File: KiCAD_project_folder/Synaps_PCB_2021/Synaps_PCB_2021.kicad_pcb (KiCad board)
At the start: 4 copper layers, 101.6 x 101.6 mm, 56 parts, among them IC2 ESP32-S2, J1 USB_C_Receptacle, U1 MAX14748BEWW+, U2 CD74HC4067M, U3 AT25DF041x-UxN-x

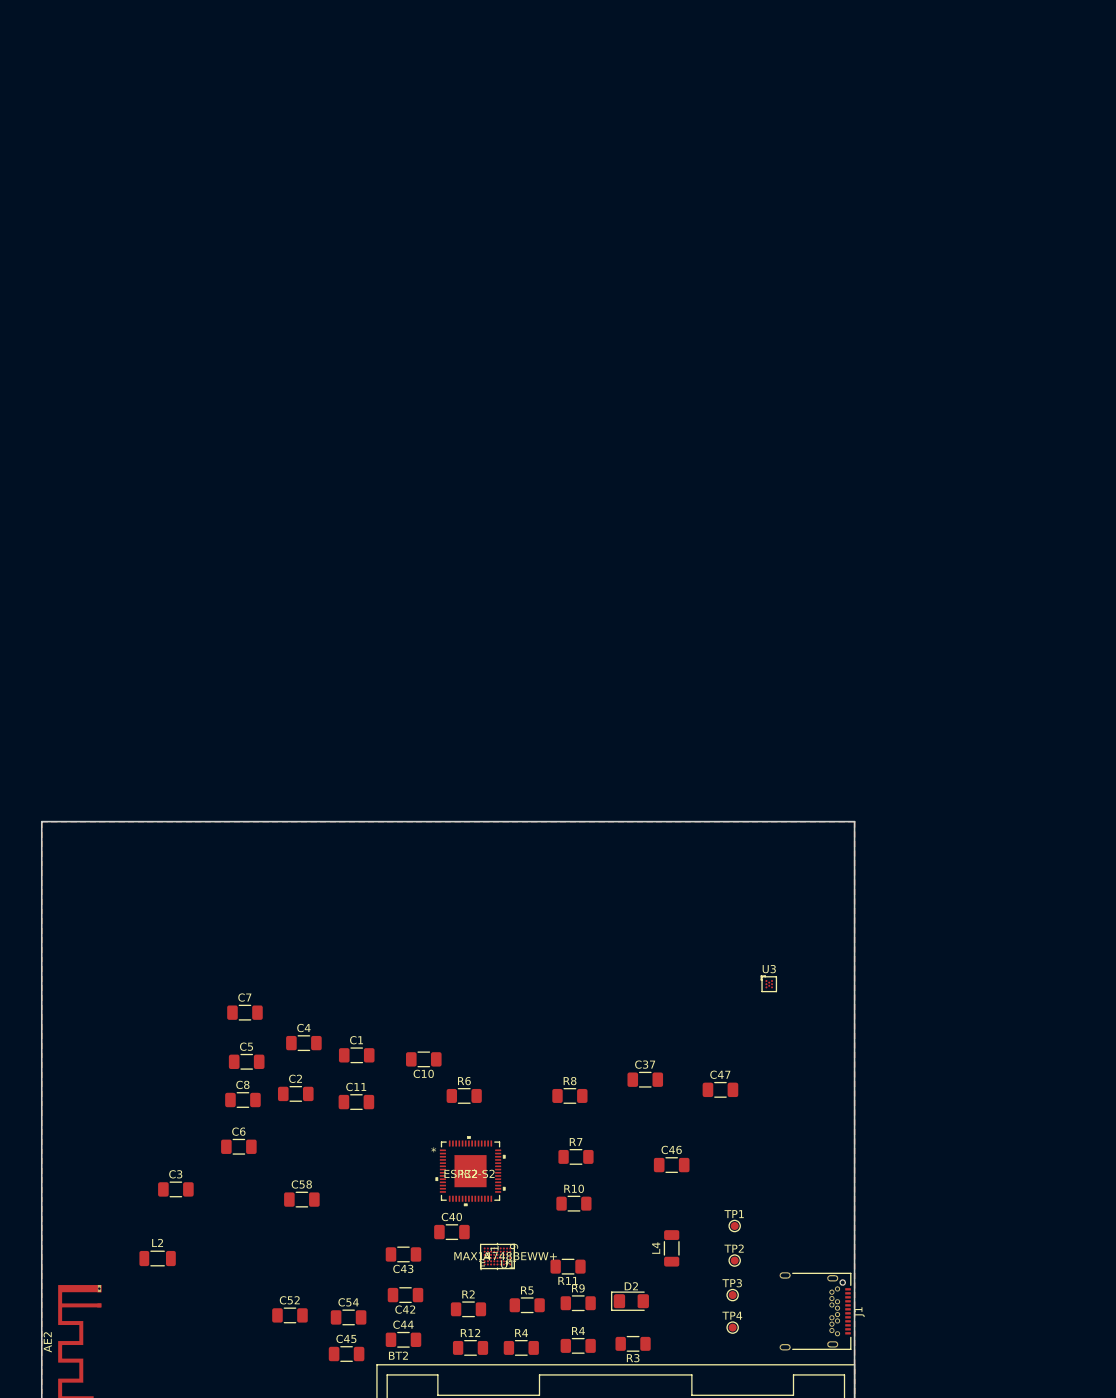
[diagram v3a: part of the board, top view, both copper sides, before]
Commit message: Updated pcb editor with the new components imported
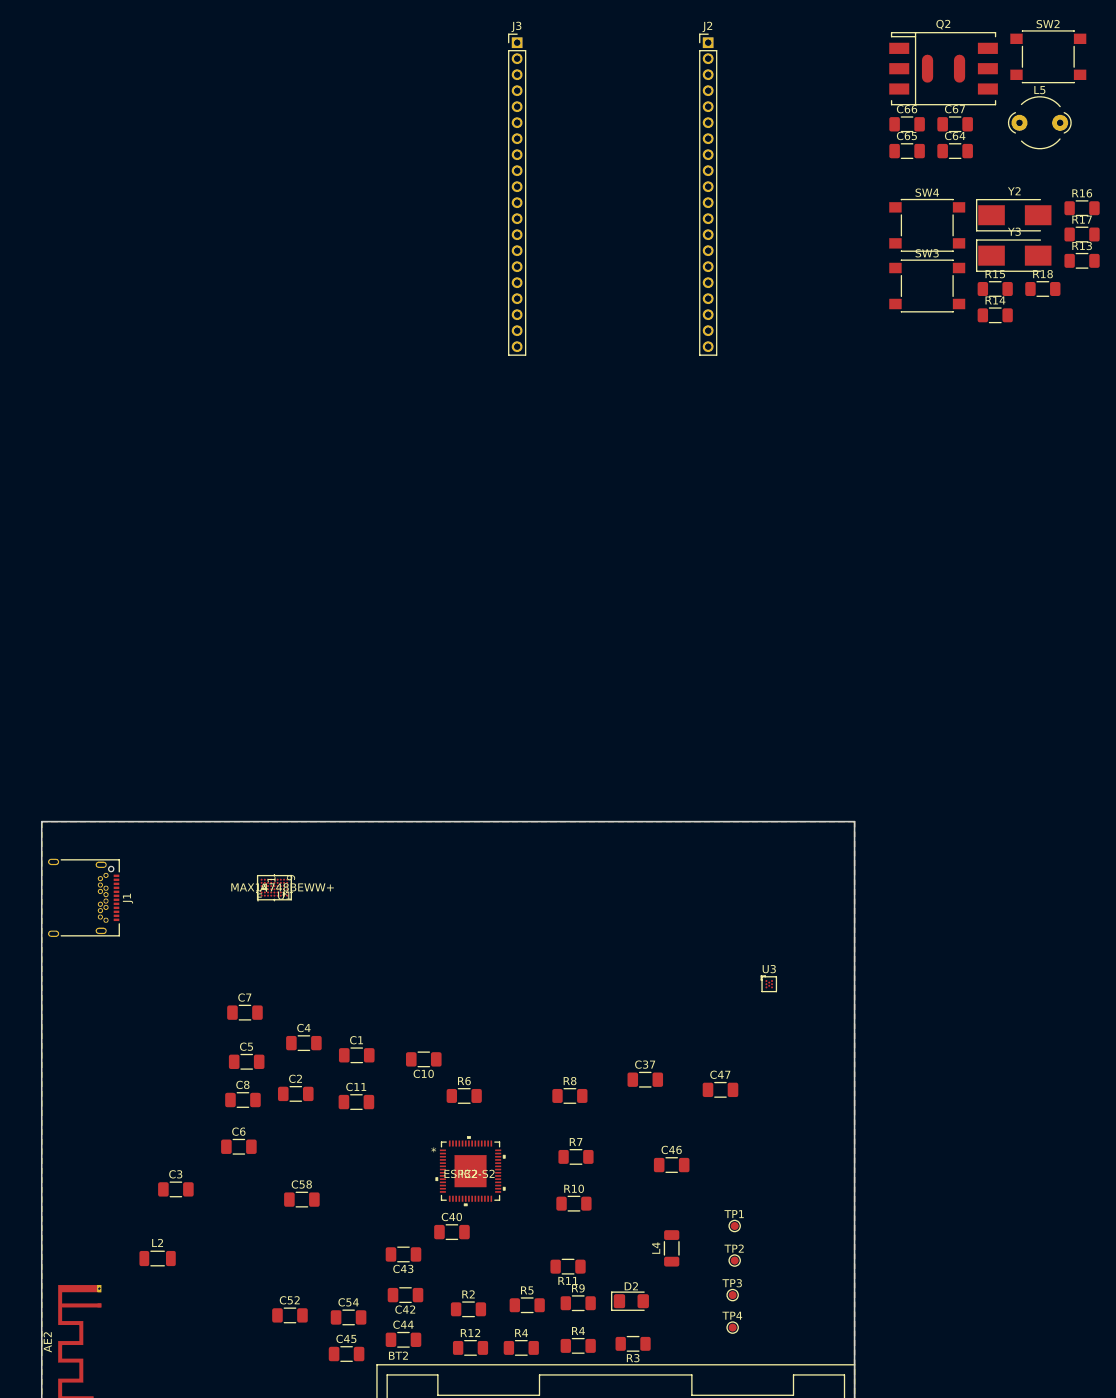
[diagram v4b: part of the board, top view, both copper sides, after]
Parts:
- added C64: 10uF, Capacitor_SMD:C_1206_3216Metric_Pad1.33x1.80mm_HandSolder, F.Cu at (208.9, -36.8)
- added C65: 0.1uF, Capacitor_SMD:C_1206_3216Metric_Pad1.33x1.80mm_HandSolder, F.Cu at (202.9, -36.8)
- added C66: 0.1uF, Capacitor_SMD:C_1206_3216Metric_Pad1.33x1.80mm_HandSolder, F.Cu at (202.9, -40.2)
- added C67: 10uF, Capacitor_SMD:C_1206_3216Metric_Pad1.33x1.80mm_HandSolder, F.Cu at (208.9, -40.2)
- added J2: Conn_01x20_MountingPin, Connector_PinHeader_2.00mm:PinHeader_1x20_P2.00mm_Vertical, F.Cu at (178.0, -50.4)
- added J3: Conn_01x20_MountingPin, Connector_PinHeader_2.00mm:PinHeader_1x20_P2.00mm_Vertical, F.Cu at (154.2, -50.4)
- added L5: L_Ferrite, Ferrite_THT:LairdTech_28C0236-0JW-10, F.Cu at (217.0, -40.4)
- added Q2: Q_PMOS_DGS, Transformer_SMD:Transformer_NF_ETAL_P2781, F.Cu at (207.5, -47.1)
- added R13: 0, Resistor_SMD:R_1206_3216Metric_Pad1.30x1.75mm_HandSolder, F.Cu at (224.8, -23.1)
- added R14: 0, Resistor_SMD:R_1206_3216Metric_Pad1.30x1.75mm_HandSolder, F.Cu at (213.9, -16.3)
- added R15: 0, Resistor_SMD:R_1206_3216Metric_Pad1.30x1.75mm_HandSolder, F.Cu at (213.9, -19.6)
- added R16: 0, Resistor_SMD:R_1206_3216Metric_Pad1.30x1.75mm_HandSolder, F.Cu at (224.8, -29.7)
- added R17: 499, Resistor_SMD:R_1206_3216Metric_Pad1.30x1.75mm_HandSolder, F.Cu at (224.8, -26.4)
- added R18: 10M, Resistor_SMD:R_1206_3216Metric_Pad1.30x1.75mm_HandSolder, F.Cu at (219.9, -19.6)
- added SW2: SW_Push, Button_Switch_SMD:SW_Push_1P1T_NO_6x6mm_H9.5mm, F.Cu at (220.6, -48.6)
- added SW3: SW_Push, Button_Switch_SMD:SW_Push_1P1T_NO_6x6mm_H9.5mm, F.Cu at (205.4, -20.0)
- added SW4: SW_Push, Button_Switch_SMD:SW_Push_1P1T_NO_6x6mm_H9.5mm, F.Cu at (205.4, -27.5)
- added Y2: Crystal_GND24, Crystal:Crystal_SMD_0603-2Pin_6.0x3.5mm_HandSoldering, F.Cu at (216.4, -28.8)
- added Y3: 32.768K, Crystal:Crystal_SMD_0603-2Pin_6.0x3.5mm_HandSoldering, F.Cu at (216.4, -23.8)
- C10: value NC -> 0.1uF/50V(10%)(NC)
- C11: value 1µF -> 0.1uF/50V(10%)(NC)
- C2: value 100nF -> 0.1uF
- C3: value 10uF -> 0.1uF
- C5: value 0.1uF -> 100pF
- C6: value 100nF -> 1uF
- C7, C8: value 0.1uF -> 12.5pF
- R3: value 4.7K -> 1M
- R6: value 0R -> 10K
- R7: value 499R -> 0
- R8: value 20K(5%) -> 0
- moved J1 105.0 mm to (99.1, 56.5)
- moved U1 53.9 mm to (123.8, 55.2)
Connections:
- net /Probes schematic/SPI3_CS3 renamed /Microcontroler/SPI3_CS3
- C10 pad 1: /Microcontroler/VDD33 -> /Microcontroler/CHIP_BOOT
- C10 pad 2: Earth -> GNDREF
- C11 pad 1: unconnected-(C11-Pad1) -> /Microcontroler/CHIP_PU
- C11 pad 2: Earth -> GNDREF
- C2 pad 1: VDDA -> +1V1
- C7 pad 2: /Probes schematic/Probes_1/Inertia Measurement Unit & ADC3/sense_+ -> /Microcontroler/XTAL_32K_P
- C8 pad 1: /Probes schematic/Probes_1/Inertia Measurement Unit & ADC3/sense_+ -> GNDREF
- C8 pad 2: /Probes schematic/Probes_1/Inertia Measurement Unit & ADC3/sense_- -> /Microcontroler/XTAL_32K_N
- R3 pad 1: Net-(R3-Pad1) -> GNDREF
- R3 pad 2: +1V1 -> Net-(J1-PadS1)
- R6 pad 1: /Microcontroler/XIN -> /Microcontroler/DAC_2
- R6 pad 2: Net-(IC2-Pad45) -> +1V1
- R7 pad 1: /Microcontroler/GPIO1 -> Net-(IC2-Pad36)
- R7 pad 2: Net-(IC2-Pad41) -> /Microcontroler/SPID
- R8 pad 1: Net-(C61-Pad1) -> Net-(IC2-Pad35)
- R8 pad 2: Net-(C61-Pad2) -> /Microcontroler/SPIQ
- U2 pad 11: /Probes schematic/SPI3_CS1 -> /Microcontroler/SPI3_CS1
- U2 pad 14: /Probes schematic/SPI3_CS2 -> /Microcontroler/SPI3_CS2

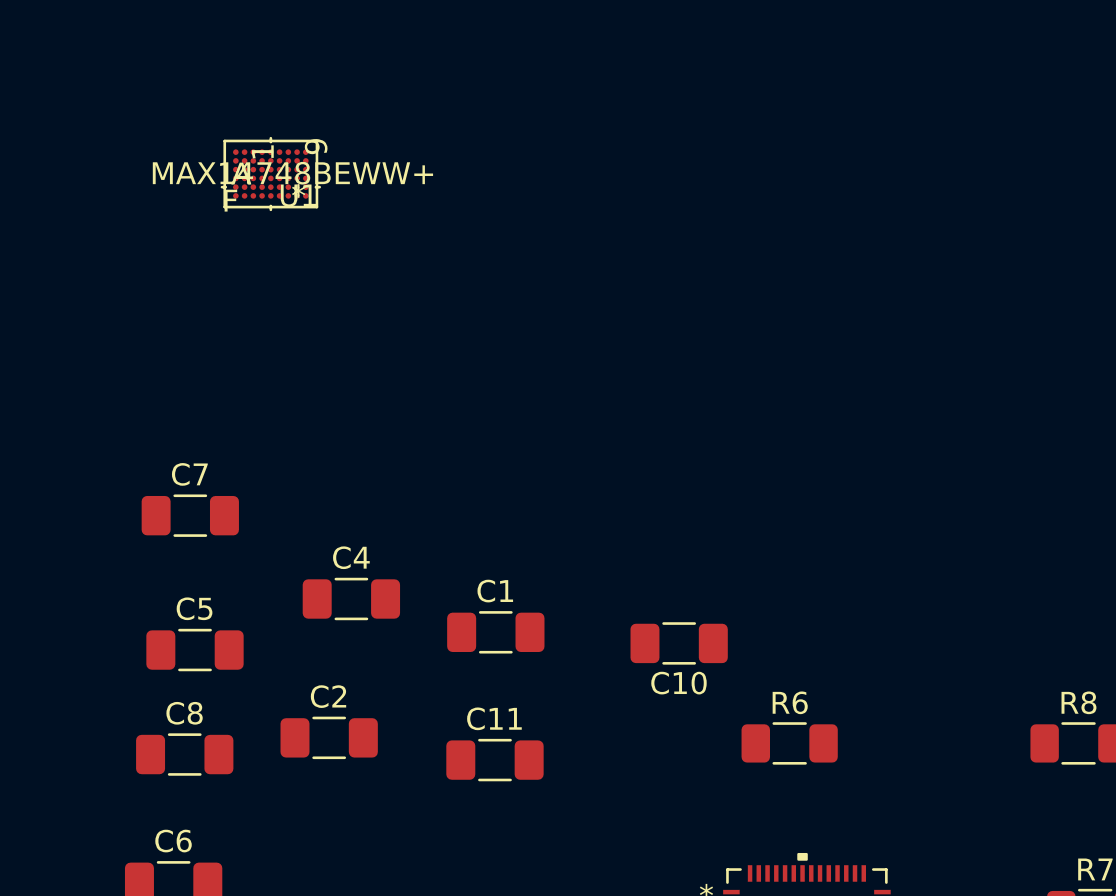
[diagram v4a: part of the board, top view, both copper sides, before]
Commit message: Fixed Board Setup to be able to trace BGA
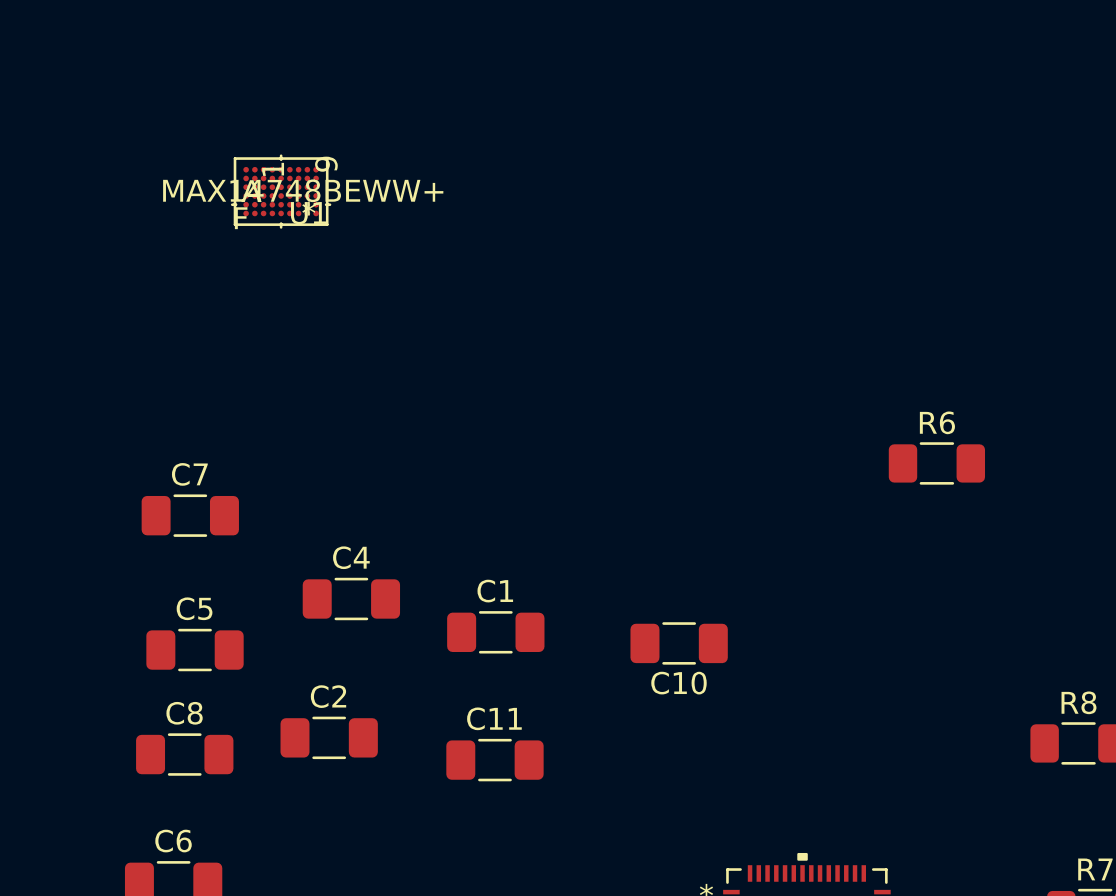
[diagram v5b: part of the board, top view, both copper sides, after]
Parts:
- moved R6 14.5 mm to (154.3, 68.5)
- moved U1 0.93 mm to (124.3, 56.0)
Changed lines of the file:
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@@
   )
   (footprint "MAX14748:MAX14748BEWW&plus_" (layer "F.Cu")
-    (at 123.825 55.245)
+    (at 124.295 56.0482)
     (property "Sheetfile" "Power_Supply.kicad_sch")
     (property "Sheetname" "Power Supply")
@@
       (effects (font (size 1 1) (thickness 0.15)))
     )
-    (fp_text user "Copyright 2021 Accelerated Designs. All rights reserved." (at 0.508 0.762) (layer "Cmts.User")
+    (fp_text user "Copyright 2021 Accelerated Designs. All rights reserved." (at 0.508 0.762) (layer "Cmts.User") hide
       (effects (font (size 0.127 0.127) (thickness 0.002)))
     )
-    (fp_text user "0.2in/5.08mm" (at 0.508 1.016) (layer "Cmts.User")
-      (effects (font (size 1 1) (thickness 0.15)))
-    )
-    (fp_text user "0.012in/0.305mm" (at 4.3942 1) (layer "Cmts.User")
-      (effects (font (size 1 1) (thickness 0.15)))
-    )
-    (fp_text user "0.15in/3.81mm" (at 1.016 1.27) (layer "Cmts.User")
-      (effects (font (size 1 1) (thickness 0.15)))
-    )
-    (fp_text user "0.016in/0.4mm" (at 4.3942 -0.8) (layer "Cmts.User")
+    (fp_text user "0.2in/5.08mm" (at 0.508 1.016) (layer "Cmts.User") hide
+      (effects (font (size 1 1) (thickness 0.15)))
+    )
+    (fp_text user "0.012in/0.305mm" (at 4.3942 1) (layer "Cmts.User") hide
+      (effects (font (size 1 1) (thickness 0.15)))
+    )
+    (fp_text user "0.15in/3.81mm" (at 1.016 1.27) (layer "Cmts.User") hide
+      (effects (font (size 1 1) (thickness 0.15)))
+    )
+    (fp_text user "0.016in/0.4mm" (at 4.3942 -0.8) (layer "Cmts.User") hide
       (effects (font (size 1 1) (thickness 0.15)))
     )
@@
     (pad "A5" smd circle locked (at 0 -1) (size 0.254 0.254) (layers "F.Cu" "F.Paste" "F.Mask")
       (net 8 "Net-(C43-Pad2)") (pinfunction "COMP") (pintype "unspecified"))
-    (pad "A6" smd circle locked (at 0.4 -1) (size 0.254 0.254) (layers "F.Cu" "F.Paste" "F.Mask")
+    (pad "A6" smd circle locked (at 0.4 -1) (size 0.254 0.254) (property pad_prop_bga) (layers "F.Cu" "F.Paste" "F.Mask")
       (net 23 "Net-(R2-Pad2)") (pinfunction "SET") (pintype "unspecified"))
     (pad "A7" smd circle locked (at 0.8 -1) (size 0.254 0.254) (layers "F.Cu" "F.Paste" "F.Mask")
@@
   )
   (footprint "Resistor_SMD:R_1206_3216Metric_Pad1.30x1.75mm_HandSolder" (layer "F.Cu")
-    (at 147.548 81.28)
+    (at 154.2796 68.4784)
     (descr "Resistor SMD 1206 (3216 Metric), square (rectangular) end terminal, IPC_7351 nominal with elongated pad for handsoldering. (Body size source: IPC-SM-782 page 72, https://www.pcb-3d.com/wordpress/wp-content/uploads/ipc-sm-782a_amendment_1_and_2.pdf), generated with kicad-footprint-generator")
     (tags "resistor handsolder")
@@
   (gr_line (start 196.342 148.59) (end 94.742 148.59) (layer "Edge.Cuts") (width 0.2))
   (zone (net 38) (net_name "GNDREF") (layer "F.Cu") (hatch edge 0.508)
-    (connect_pads (clearance 0.508))
-    (min_thickness 0.254) (filled_areas_thickness no)
+    (priority 4)
+    (connect_pads (clearance 0.01))
+    (min_thickness 0.2) (filled_areas_thickness no)
     (fill yes (thermal_gap 0.508) (thermal_bridge_width 0.508))
     (polygon

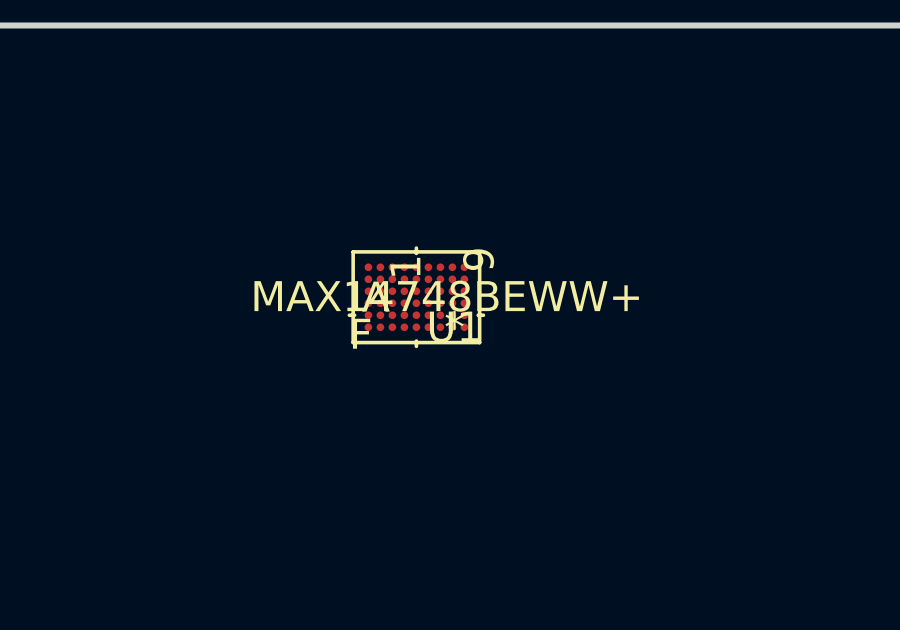
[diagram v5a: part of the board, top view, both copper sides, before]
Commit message: Testing to see with Design Rule Check if saved
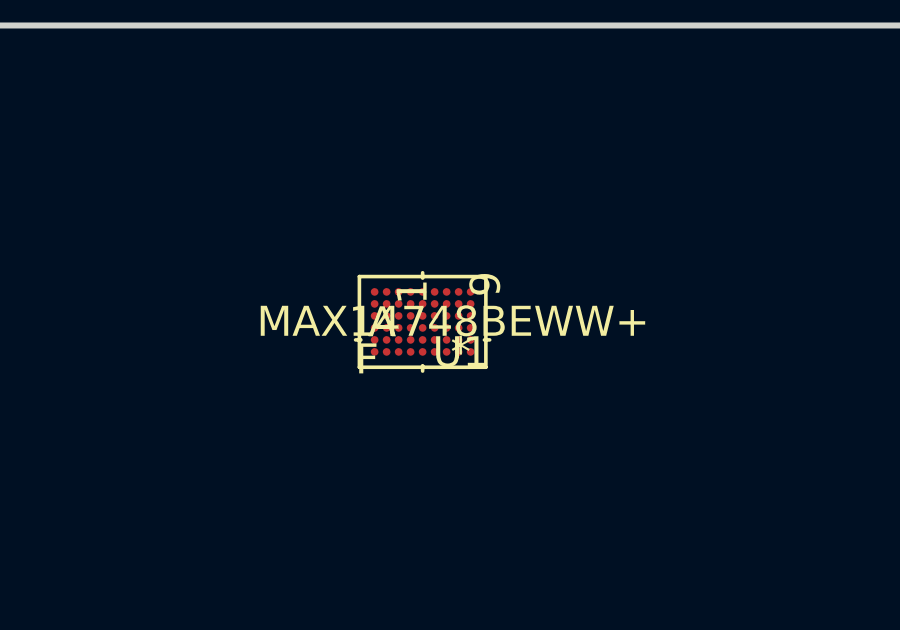
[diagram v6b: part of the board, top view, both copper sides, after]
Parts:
- moved U1 0.85 mm to (124.5, 56.9)
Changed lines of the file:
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@@
   )
   (footprint "MAX14748:MAX14748BEWW&plus_" (layer "F.Cu")
-    (at 124.295 56.0482)
+    (at 124.5031 56.8706)
     (property "Sheetfile" "Power_Supply.kicad_sch")
     (property "Sheetname" "Power Supply")

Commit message: Worked on MAX tracking for PCB
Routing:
- net /Microcontroler/I2CEXT0_SCL_out: track 0.00 -> 142.2 mm
- net /Power Supply/V_BAT: track 0.00 -> 139.6 mm
- net /Power Supply/VCONN: track 0.00 -> 119.6 mm
- net Net-(R11-Pad1): track 0.00 -> 109.9 mm
- net /Power Supply/CC1: track 0.00 -> 106.3 mm
- net Net-(C46-Pad1): track 0.00 -> 90.8 mm
- net /Microcontroler/LED_PMIC: track 0.00 -> 78.0 mm
- net /Power Supply/TPU: track 0.00 -> 62.1 mm
- net Net-(J1-PadS1): track 0.00 -> 20.9 mm
- net /Power Supply/CHGIN: track 0.00 -> 5.42 mm
- net Net-(D2-Pad1): track 0.00 -> 3.71 mm
- net +1V1: track 0.00 -> 2.19 mm
- net /Microcontroler/*INT: track 0.00 -> 1.57 mm
- net /Power Supply/LX: track 0.00 -> 1.45 mm
- net Net-(Q2-Pad3): track 0.00 -> 1.20 mm
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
